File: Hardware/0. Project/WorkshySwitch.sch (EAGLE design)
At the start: 22 parts, among them IC1 LM1117-3.3, J1 ICSP, K1 G3MB-202P, T1 BC848, U1 HLK-PM01, U2 ATMEGA328P-AU

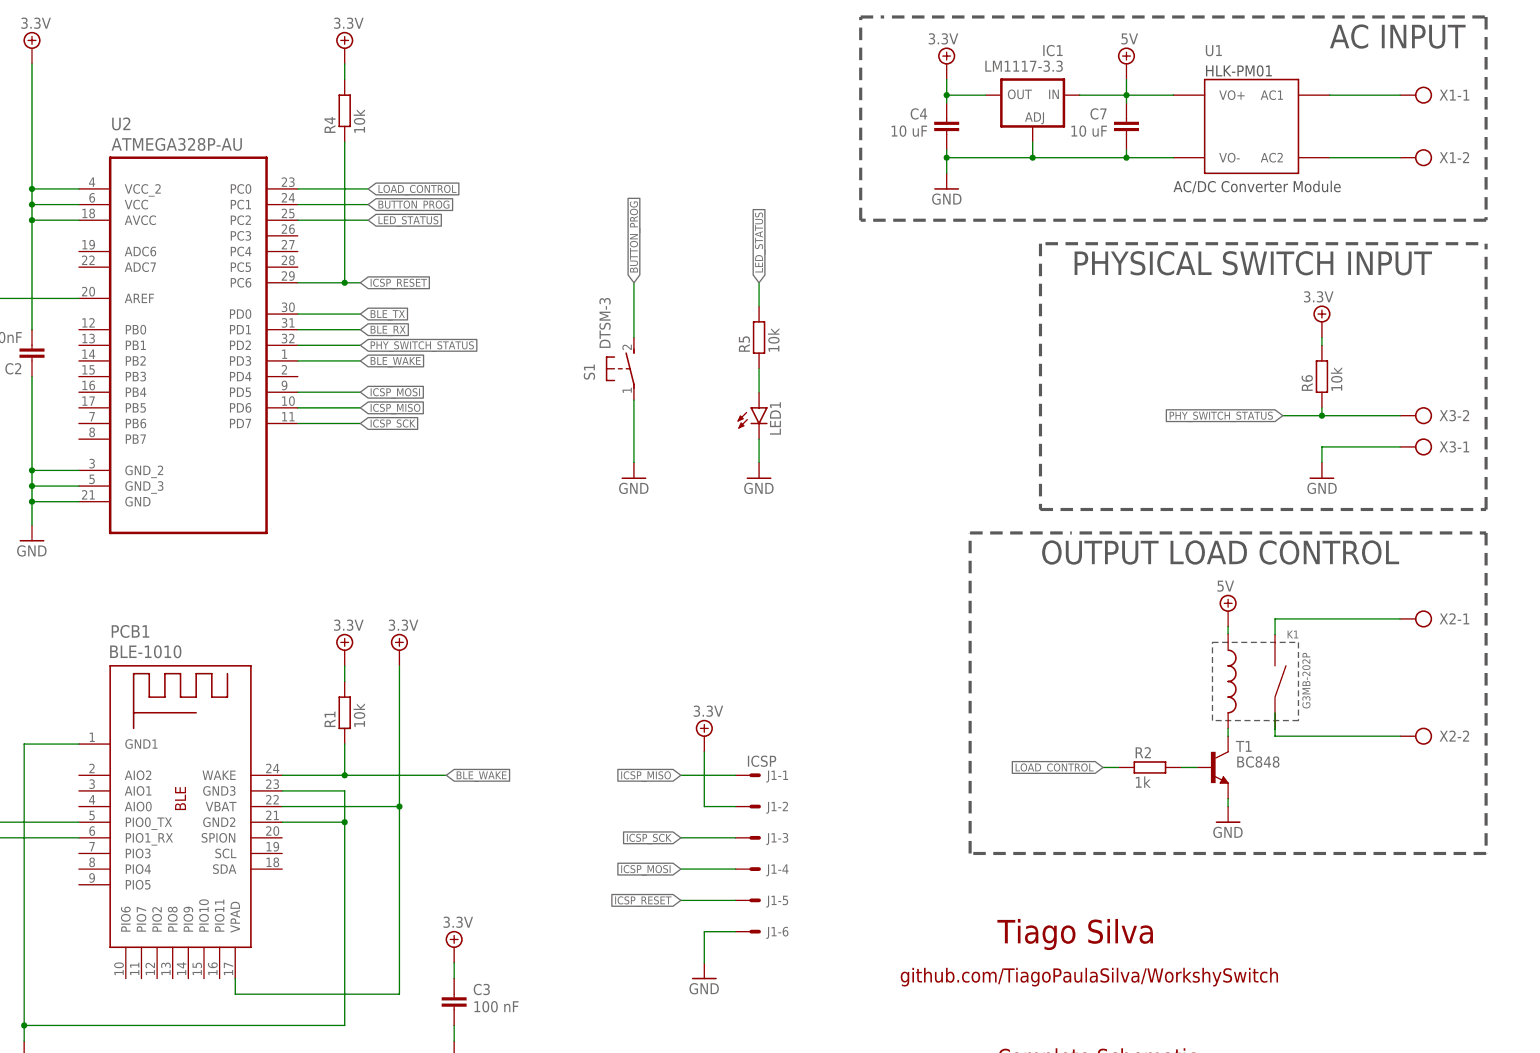
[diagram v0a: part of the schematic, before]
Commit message: Protect circuit added
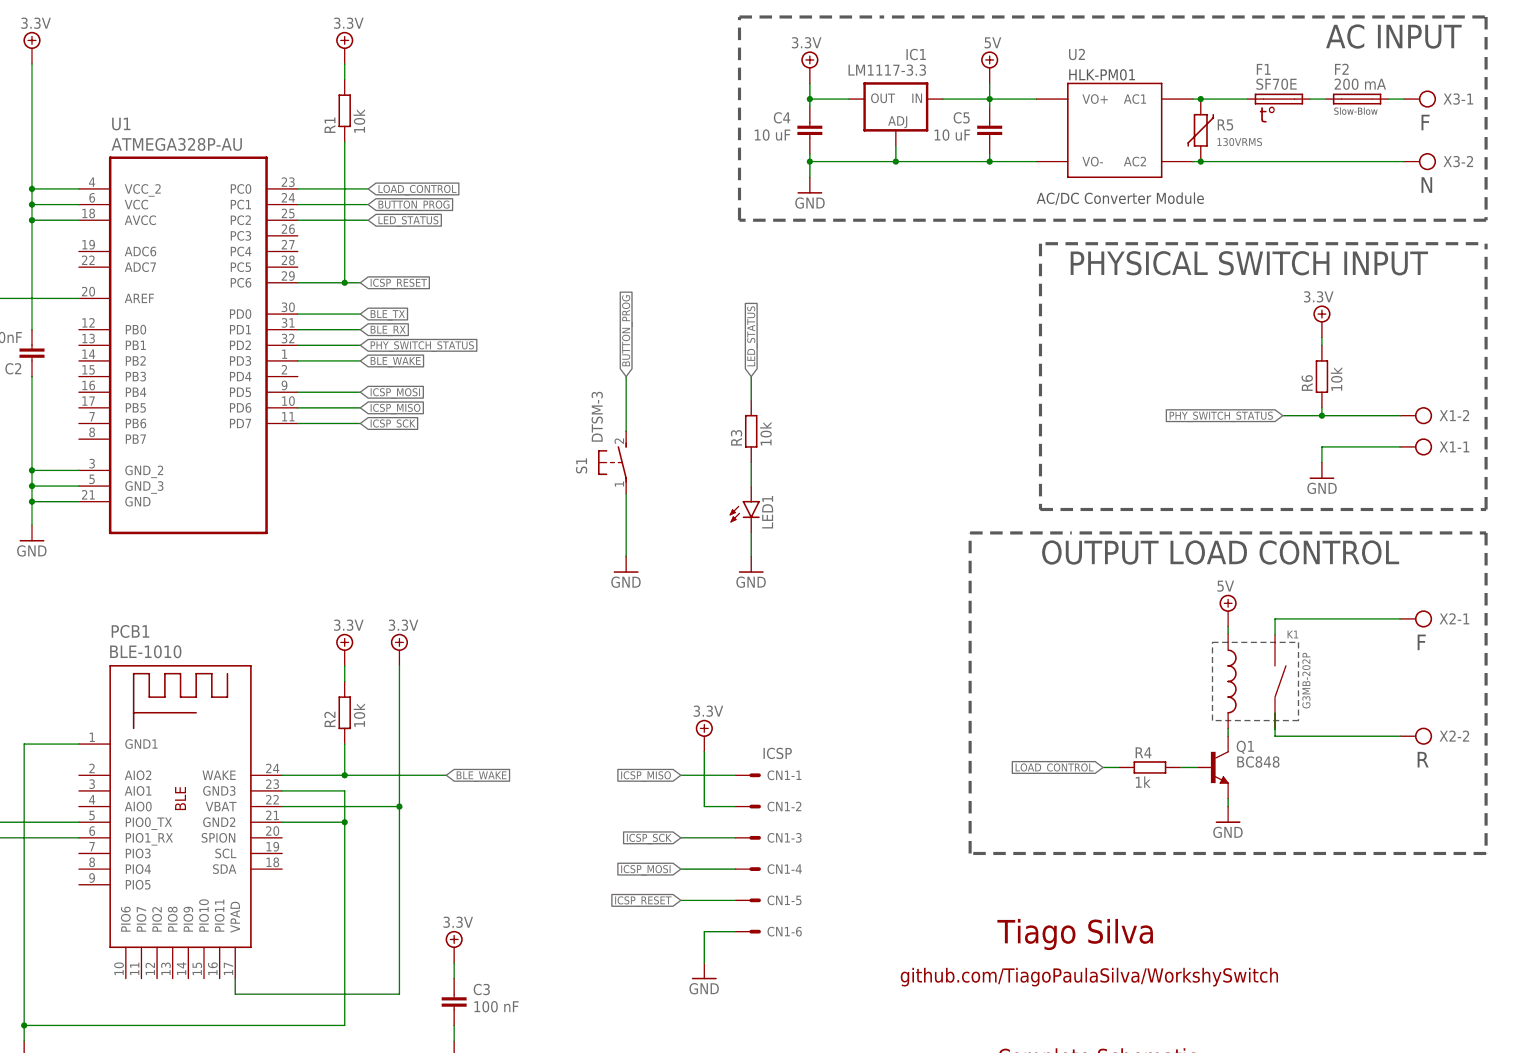
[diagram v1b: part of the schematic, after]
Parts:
- removed C7: 10 uF, rcl:C-EUC0603
- added C5: 10 uF, rcl:C-EUC0603
- added F1: SF70E, Thermal Fuse:LITTLEFUSE
- added F2: 200 mA, fuse:QPL
- added R3: 10k, rcl:R-EU_R0603
- R2: value 1k -> 10k
- R4: value 10k -> 1k
- R5: value 10k -> 130VRMS; device rcl:R-EU_R0603 -> varistor:VARISTORS05K11
- U1: value HLK-PM01 -> ATMEGA328P-AU; device HLK-PM01:HLK-PM01 -> Atmel_By_element14_Batch_1-00:ATMEGA328P-AU
- U2: value ATMEGA328P-AU -> HLK-PM01; device Atmel_By_element14_Batch_1-00:ATMEGA328P-AU -> HLK-PM01:HLK-PM01
- renumbered J1 to CN1, T1 to Q1
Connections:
- new net N$4: F1.1, R5.1, U2.AC1
- new net N$9: F1.2, F2.1
- net 3.3V: now also R1.2, R2.1, U1.AVCC, U1.VCC, U1.VCC_2; no longer R1.1, R4.2, U2.AVCC, U2.VCC, U2.VCC_2
- net 5V: now also C5.1, U2.VO+; no longer C7.1, U1.VO+
- net BLE_RX: now also U1.PD1; no longer U2.PD1
- net BLE_TX: now also U1.PD0; no longer U2.PD0
- net BLE_WAKE: now also R2.2, U1.PD3; no longer R1.2, U2.PD3
- net BUTTON_PROG: now also U1.PC1; no longer U2.PC1
- net GND: now also C5.2, U1.GND, U1.GND_2, U1.GND_3, U2.VO-, X1-1.KL; no longer C7.2, U1.VO-, U2.GND, U2.GND_2, U2.GND_3, X3-1.KL
- net ICSP_MISO: now also U1.PD6; no longer U2.PD6
- net ICSP_MOSI: now also U1.PD5; no longer U2.PD5
- net ICSP_RESET: now also R1.1, U1.PC6; no longer R4.1, U2.PC6
- net ICSP_SCK: now also U1.PD7; no longer U2.PD7
- net LED_STATUS: now also R3.1, U1.PC2; no longer R5.1, U2.PC2
- net LOAD_CONTROL: now also R4.1, U1.PC0; no longer R2.1, U2.PC0
- net N$1: now also R3.2; no longer R5.2
- net N$11: now also U1.AREF; no longer U2.AREF
- net N$2: now also F2.2, X3-1.KL; no longer U1.AC1, X1-1.KL
- net N$3: now also R5.2, U2.AC2, X3-2.KL; no longer U1.AC2, X1-2.KL
- net N$6: now also R4.2; no longer R2.2
- net PHY_SWITCH_STATUS: now also U1.PD2, X1-2.KL; no longer U2.PD2, X3-2.KL
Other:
- note added: "F"
- note added: "N"
- note added: "R"
- note added: "Slow-Blow"
- moved on the sheet: C4, IC1, LED1, R1, R2, R4, S1, X1-1, X1-2, X3-1, X3-2

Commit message: PCB layout under dev
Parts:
- CN1: device con-molex:22-05-7068-06 -> pinhead:PINHD-1X6
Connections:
- net 3.3V: now also CN1.2; no longer CN1-2.S
- net GND: now also CN1.6; no longer CN1-6.S
- net ICSP_MISO: now also CN1.1; no longer CN1-1.S
- net ICSP_MOSI: now also CN1.4; no longer CN1-4.S
- net ICSP_RESET: now also CN1.5; no longer CN1-5.S
- net ICSP_SCK: now also CN1.3; no longer CN1-3.S
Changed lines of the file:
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@@
 <setting verticaltext="up"/>
 </settings>
-<grid distance="0.05" unitdist="inch" unit="inch" style="lines" multiple="1" display="no" altdistance="0.01" altunitdist="inch" altunit="inch"/>
+<grid distance="0.1" unitdist="inch" unit="inch" style="lines" multiple="1" display="no" altdistance="0.01" altunitdist="inch" altunit="inch"/>
 <layers>
 <layer number="1" name="Top" color="4" fill="1" visible="no" active="no"/>
@@
 <part name="GND1" library="supply1" library_urn="urn:adsk.eagle:library:371" deviceset="GND" device=""/>
 <part name="C2" library="rcl" library_urn="urn:adsk.eagle:library:334" deviceset="C-EU" device="C0603" package3d_urn="urn:adsk.eagle:package:23616/2" value="100nF"/>
-<part name="CN1" library="con-molex" library_urn="urn:adsk.eagle:library:165" deviceset="22-?-06" device="05-7068" package3d_urn="urn:adsk.eagle:package:8078652/1" value="ICSP"/>
 <part name="SUPPLY6" library="supply2" library_urn="urn:adsk.eagle:library:372" deviceset="+4.1V" device="" value="3.3V"/>
 <part name="GND6" library="supply1" library_urn="urn:adsk.eagle:library:371" deviceset="GND" device=""/>
@@
 <part name="F1" library="Thermal Fuse" deviceset="LITTLEFUSE" device="" package3d_urn="urn:adsk.eagle:package:14064/1" value="SF70E"/>
 <part name="R5" library="varistor" library_urn="urn:adsk.eagle:library:410" deviceset="VARISTOR" device="S05K11" package3d_urn="urn:adsk.eagle:package:30524/1" value="130VRMS"/>
+<part name="CN1" library="pinhead" library_urn="urn:adsk.eagle:library:325" deviceset="PINHD-1X6" device="" package3d_urn="urn:adsk.eagle:package:22472/2" value="ICSP"/>
 </parts>
 <sheets>
@@
 <attribute name="VALUE" x="23.876" y="125.349" size="1.778" layer="96" rot="R180"/>
 </instance>
-<instance part="CN1" gate="-1" x="142.24" y="53.34" smashed="yes">
-<attribute name="NAME" x="144.78" y="52.578" size="1.524" layer="95"/>
-<attribute name="VALUE" x="144.018" y="56.007" size="1.778" layer="96"/>
-</instance>
-<instance part="CN1" gate="-2" x="142.24" y="48.26" smashed="yes">
-<attribute name="NAME" x="144.78" y="47.498" size="1.524" layer="95"/>
-</instance>
-<instance part="CN1" gate="-3" x="142.24" y="43.18" smashed="yes">
-<attribute name="NAME" x="144.78" y="42.418" size="1.524" layer="95"/>
-</instance>
-<instance part="CN1" gate="-4" x="142.24" y="38.1" smashed="yes">
-<attribute name="NAME" x="144.78" y="37.338" size="1.524" layer="95"/>
-</instance>
-<instance part="CN1" gate="-5" x="142.24" y="33.02" smashed="yes">
-<attribute name="NAME" x="144.78" y="32.258" size="1.524" layer="95"/>
-</instance>
-<instance part="CN1" gate="-6" x="142.24" y="27.94" smashed="yes">
-<attribute name="NAME" x="144.78" y="27.178" size="1.524" layer="95"/>
-</instance>
-<instance part="SUPPLY6" gate="P" x="134.62" y="59.69" smashed="yes">
-<attribute name="VALUE" x="132.715" y="62.865" size="1.778" layer="96"/>
-</instance>
-<instance part="GND6" gate="1" x="134.62" y="20.32" smashed="yes">
-<attribute name="VALUE" x="132.08" y="17.78" size="1.778" layer="96"/>
+<instance part="SUPPLY6" gate="P" x="134.62" y="54.61" smashed="yes">
+<attribute name="VALUE" x="132.715" y="57.785" size="1.778" layer="96"/>
+</instance>
+<instance part="GND6" gate="1" x="134.62" y="22.86" smashed="yes">
+<attribute name="VALUE" x="132.08" y="20.32" size="1.778" layer="96"/>
 </instance>
 <instance part="C5" gate="G$1" x="180.975" y="159.385" smashed="yes" rot="MR0">
@@
 <attribute name="NAME" x="217.805" y="158.115" size="1.778" layer="95"/>
 <attribute name="VALUE" x="217.805" y="155.575" size="1.27" layer="96"/>
+</instance>
+<instance part="CN1" gate="A" x="144.78" y="38.1" smashed="yes">
+<attribute name="NAME" x="138.43" y="48.895" size="1.778" layer="95"/>
+<attribute name="VALUE" x="138.43" y="27.94" size="1.778" layer="96"/>
 </instance>
 </instances>
@@
 </segment>
 <segment>
-<pinref part="CN1" gate="-6" pin="S"/>
-<pinref part="GND6" gate="1" pin="GND"/>
-<wire x1="139.7" y1="27.94" x2="134.62" y2="27.94" width="0.1524" layer="91"/>
-<wire x1="134.62" y1="27.94" x2="134.62" y2="22.86" width="0.1524" layer="91"/>
-</segment>
-<segment>
 <pinref part="U2" gate="G$1" pin="VO-"/>
 <wire x1="188.595" y1="153.035" x2="180.975" y2="153.035" width="0.1524" layer="91"/>
@@
 <wire x1="234.95" y1="106.68" x2="234.95" y2="104.14" width="0.1524" layer="91"/>
 </segment>
+<segment>
+<pinref part="CN1" gate="A" pin="6"/>
+<wire x1="142.24" y1="33.02" x2="134.62" y2="33.02" width="0.1524" layer="91"/>
+<pinref part="GND6" gate="1" pin="GND"/>
+<wire x1="134.62" y1="33.02" x2="134.62" y2="25.4" width="0.1524" layer="91"/>
+</segment>
 </net>
 <net name="BLE_RX" class="0">
@@
 </segment>
 <segment>
-<label x="130.81" y="43.18" size="1.27" layer="95" ratio="10" rot="R180" xref="yes"/>
-<pinref part="CN1" gate="-3" pin="S"/>
-<wire x1="139.7" y1="43.18" x2="130.81" y2="43.18" width="0.1524" layer="91"/>
+<label x="130.81" y="40.64" size="1.27" layer="95" ratio="10" rot="R180" xref="yes"/>
+<pinref part="CN1" gate="A" pin="3"/>
+<wire x1="142.24" y1="40.64" x2="130.81" y2="40.64" width="0.1524" layer="91"/>
 </segment>
 </net>
@@
 <segment>
 <label x="130.81" y="38.1" size="1.27" layer="95" ratio="10" rot="R180" xref="yes"/>
-<pinref part="CN1" gate="-4" pin="S"/>
-<wire x1="139.7" y1="38.1" x2="130.81" y2="38.1" width="0.1524" layer="91"/>
+<pinref part="CN1" gate="A" pin="4"/>
+<wire x1="142.24" y1="38.1" x2="130.81" y2="38.1" width="0.1524" layer="91"/>
 </segment>
 </net>
@@
 </segment>
 <segment>
-<pinref part="CN1" gate="-2" pin="S"/>
 <pinref part="SUPPLY6" gate="P" pin="+4.1V"/>
-<wire x1="139.7" y1="48.26" x2="134.62" y2="48.26" width="0.1524" layer="91"/>
-<wire x1="134.62" y1="48.26" x2="134.62" y2="57.15" width="0.1524" layer="91"/>
+<wire x1="134.62" y1="43.18" x2="134.62" y2="52.07" width="0.1524" layer="91"/>
+<pinref part="CN1" gate="A" pin="2"/>
+<wire x1="142.24" y1="43.18" x2="134.62" y2="43.18" width="0.1524" layer="91"/>
 </segment>
 <segment>
@@
 </segment>
 <segment>
-<label x="130.81" y="33.02" size="1.27" layer="95" ratio="10" rot="R180" xref="yes"/>
-<pinref part="CN1" gate="-5" pin="S"/>
-<wire x1="139.7" y1="33.02" x2="130.81" y2="33.02" width="0.1524" layer="91"/>
+<label x="130.81" y="35.56" size="1.27" layer="95" ratio="10" rot="R180" xref="yes"/>
+<pinref part="CN1" gate="A" pin="5"/>
+<wire x1="142.24" y1="35.56" x2="130.81" y2="35.56" width="0.1524" layer="91"/>
 </segment>
 </net>
 <net name="ICSP_MISO" class="0">
 <segment>
-<label x="130.81" y="53.34" size="1.27" layer="95" ratio="10" rot="R180" xref="yes"/>
-<pinref part="CN1" gate="-1" pin="S"/>
-<wire x1="139.7" y1="53.34" x2="130.81" y2="53.34" width="0.1524" layer="91"/>
-</segment>
-<segment>
+<label x="130.81" y="45.72" size="1.27" layer="95" ratio="10" rot="R180" xref="yes"/>
+<pinref part="CN1" gate="A" pin="1"/>
+<wire x1="142.24" y1="45.72" x2="130.81" y2="45.72" width="0.1524" layer="91"/>
+</segment>
+<segment>

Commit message: New hardware design approch
- The previous approach would be too large.
- Now, MCU and BLE module don't exists anymore.
- A new MCU with embedded BLE was added: CC2541.
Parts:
- removed C3: 100 nF, rcl:C-EUC0603
- removed C4: 10 uF, rcl:C-EUC0603
- removed CN1: ICSP, pinhead:PINHD-1X6
- removed PCB1: BLE-1010, BLE-1010:BLE-1010
- removed Q1: BC848, transistor:BC848
- removed R1, R6: 10k, rcl:R-EU_R0603
- removed U1: ATMEGA328P-AU, Atmel_By_element14_Batch_1-00:ATMEGA328P-AU
- added A3: 50R, PCB Antenna:ANTENNA
- added C18, C19: 18pF, smd-ipc:C0402
- added C21, C22, C24: 1pF, smd-ipc:C0402
- added C23: DNM, smd-ipc:C0402
- added C25: 220pF, smd-ipc:C0402
- added C26, C28, C29, C30, C31: 100nF, smd-ipc:C0402
- added C27, C32: 1uF, smd-ipc:C0402
- added C33, C34: 12pF, smd-ipc:C0402
- added C35, C36: 15pF, smd-ipc:C0402
- added C6: 2.2uF, smd-ipc:C0402
- added C7: 100nF, rcl:C-EUC0603
- added C9: 100n, smd-ipc:C0402
- added JP2: (no value), pinhead:PINHD-2X5
- added L1, L2: 2nH, smd-ipc:L0402
- added L3: 1nH, smd-ipc:L0402
- added L4: 3nH, smd-ipc:L0402
- added L5: BLM15HG102SN1D, smd-ipc:L0402
- added Q3: 32-MHz, crystal:FA-128
- added Q4: 32.768-kHz, crystal-geyer_V1_0:KX-327-NHF
- added R10: 56k, smd-ipc:R0402
- added R7: 10k, smd-ipc:R0402
- added R8: 2.7k, smd-ipc:R0402
- added SJ1: (no value), jumper:SJ
- added T1: BC848, transistor:BC848
- added U3: CC2541, CC2541F256RHAT:CC2541F256RHAT
- C2: value 100nF -> 10uF
- C5: value 10 uF -> 10uF
- R2: device rcl:R-EU_R0603 -> smd-ipc:R0402
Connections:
- removed net BLE_RX: PCB1.PIO1_RX, U1.PD1
- removed net BLE_TX: PCB1.PIO0_TX, U1.PD0
- removed net BLE_WAKE: PCB1.WAKE, R2.2, U1.PD3
- removed net ICSP_MISO: CN1.1, U1.PD6
- removed net ICSP_MOSI: CN1.4, U1.PD5
- removed net ICSP_RESET: CN1.5, R1.1, U1.PC6
- removed net ICSP_SCK: CN1.3, U1.PD7
- new net +4.1V: C25.1, C26.1, C28.1, C29.1, C30.1, C31.1, C32.1, C6.1, JP2.2, L5.1, R2.2, R7.2, SJ1.2, U3.AVDD1, U3.AVDD2, U3.AVDD3, U3.AVDD4, U3.AVDD5, U3.AVDD6, U3.DVDD1, U3.DVDD2
- new net DEBUG_CLK: JP2.3, U3.P2_2
- new net DEBUG_DATA: JP2.4, U3.P2_1
- new net DEBUG_RESET: JP2.7, R8.1
- new net MCU_RESET: C9.1, R8.2, U3.RESET_N
- new net N$10: JP2.9, SJ1.1
- new net N$12: C19.1, C22.2, L1.1
- new net N$13: C22.1, C23.2, L2.2, L3.1
- new net N$14: C19.2, U3.RF_N
- new net N$15: C18.2, C21.1, L2.1
- new net N$44: C24.1, L3.2, L4.1
- new net N$45: A3.FEED, L4.2
- new net N$46: C27.1, U3.DCOUPL
- new net N$47: R10.2, U3.R_BIAS
- new net N$48: C33.1, Q3.1, U3.XOSC_Q2
- new net N$49: C34.1, Q3.3, U3.XOSC_Q1
- new net N$50: C35.1, Q4.1, U3.P2_4/OSC32K_Q1
- new net N$51: C36.1, Q4.2, U3.P2_3/OSC32K_Q2
- net 3.3V: now also C1.1, C2.1, L5.2; no longer C2.2, C3.1, C4.1, CN1.2, PCB1.VBAT, PCB1.VPAD, R1.2, R2.1, R6.1, U1.AVCC, U1.VCC, U1.VCC_2
- net 5V: now also C7.1
- net BUTTON_PROG: now also R2.1, U3.P1_2; no longer U1.PC1
- net GND: now also A3.GND, C1.2, C2.2, C21.2, C23.1, C24.2, C25.2, C26.2, C27.2, C28.2, C29.2, C30.2, C31.2, C32.2, C33.2, C34.2, C35.2, C36.2, C6.2, C7.2, C9.2, JP2.1, L1.2, Q3.2, Q3.4, R10.1, T1.E, U3.GND@1, U3.SCL, U3.SDA; no longer C1.1, C2.1, C3.2, C4.2, CN1.6, PCB1.GND1, PCB1.GND2, PCB1.GND3, Q1.E, U1.GND, U1.GND_2, U1.GND_3
- net LED_STATUS: now also U3.P1_0; no longer U1.PC2
- net LOAD_CONTROL: now also U3.P1_1; no longer U1.PC0
- net N$11: now also C18.1, U3.RF_P; no longer C1.2, U1.AREF
- net N$5: now also T1.C; no longer Q1.C
- net N$6: now also T1.B; no longer Q1.B
- net PHY_SWITCH_STATUS: now also R7.1, U3.P1_3; no longer R6.2, U1.PD2
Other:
- note added: "(2.0 × 1.6 mm)"
- note added: "(3.2×1.5 mm)"
- note added: "1000Ω @ 100MHz"
- note added: "IN-CIRCUIT SERIAL PROGRAMING"
- note added: "POWER SUPPLY"
- note added: "Power the target from debugger"
- note added: "USER INTERFACE"
- note removed: "AC INPUT"
- moved on the sheet: C1, C2, C5, F1, F2, IC1, K1, LED1, R2, R3, R4, R5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

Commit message: Reduced number of PTR connectors
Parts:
- removed X2: (no value), con-ptr500:AK500/2-H
- X3: device con-ptr500:AK500/2-H -> con-ptr500:AK500/3-H
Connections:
- removed net N$2: F2.2, X3-1.KL
- removed net N$7: K1.L1, X2-1.KL
- new net L1_PHASE: F2.2, K1.L1, X3-1.KL
- net N$8: now also X3-3.KL; no longer X2-2.KL
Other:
- note added: "COM"
- note added: "L1"
- note removed: "F"
- note removed: "R"
- moved on the sheet: C1, C2, C5, C6, C7, F1, F2, IC1, L5, R5, U2
